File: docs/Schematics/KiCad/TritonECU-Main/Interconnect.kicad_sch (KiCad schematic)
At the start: 3 parts, among them J1 EEC-V 104

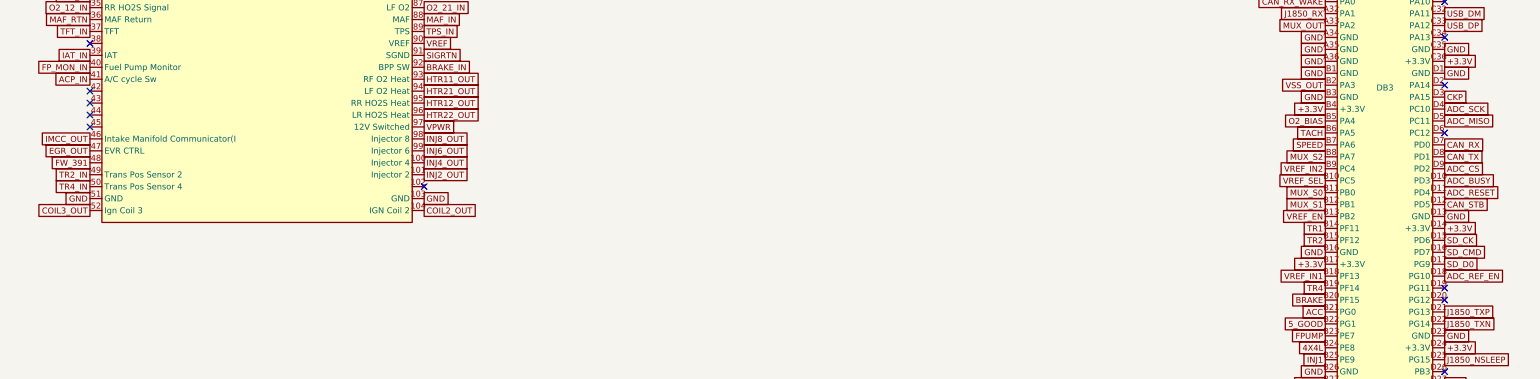
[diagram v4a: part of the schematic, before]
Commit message: Carrier: Comms sheet (SCP, CAN, USB-C, microSD)
SCP: DRV8837 (coast = passive, nSLEEP 10k low), 100R per line, NUP2105L;
TLV7031 RX with the corrected 100k:100k divider to GND, MM3Z3V3 clamps,
4.7M hysteresis, 100R + SMF3.3A out. CAN: TJA1042T/3, RXD also to PA0
WKUP1, split termination 2 x 60.4R + 4.7n, NUP2105L; bus on EEC-V 42/43
(added terminals, unused cavities). USB-C device (USB4105, 5.1k CC,
USBLC6-2SC6, VBUS sense). microSD Molex 104031 on SDMMC2 1-bit, powered
through a TPS22917 on SD_PWR_EN (PG11): 3.3 V is always on.

USB-C on the right board edge; microSD parked off-board (wider than the
free strip). Scoped DRC rule for the USB4105 land pattern.

Co-Authored-By: Claude Opus 5.5 <noreply@anthropic.com>
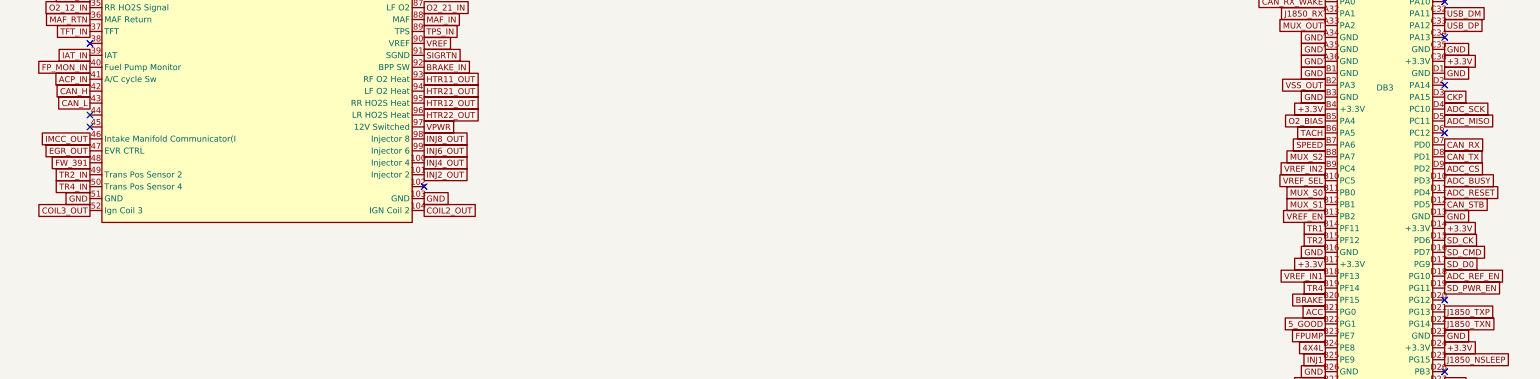
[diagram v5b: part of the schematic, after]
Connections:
- net CAN_H: now reaches J1.42
- net CAN_L: now reaches J1.43
- net SD_PWR_EN: now reaches DB3.D19 (PG11)
- no-connect marks 38 -> 35

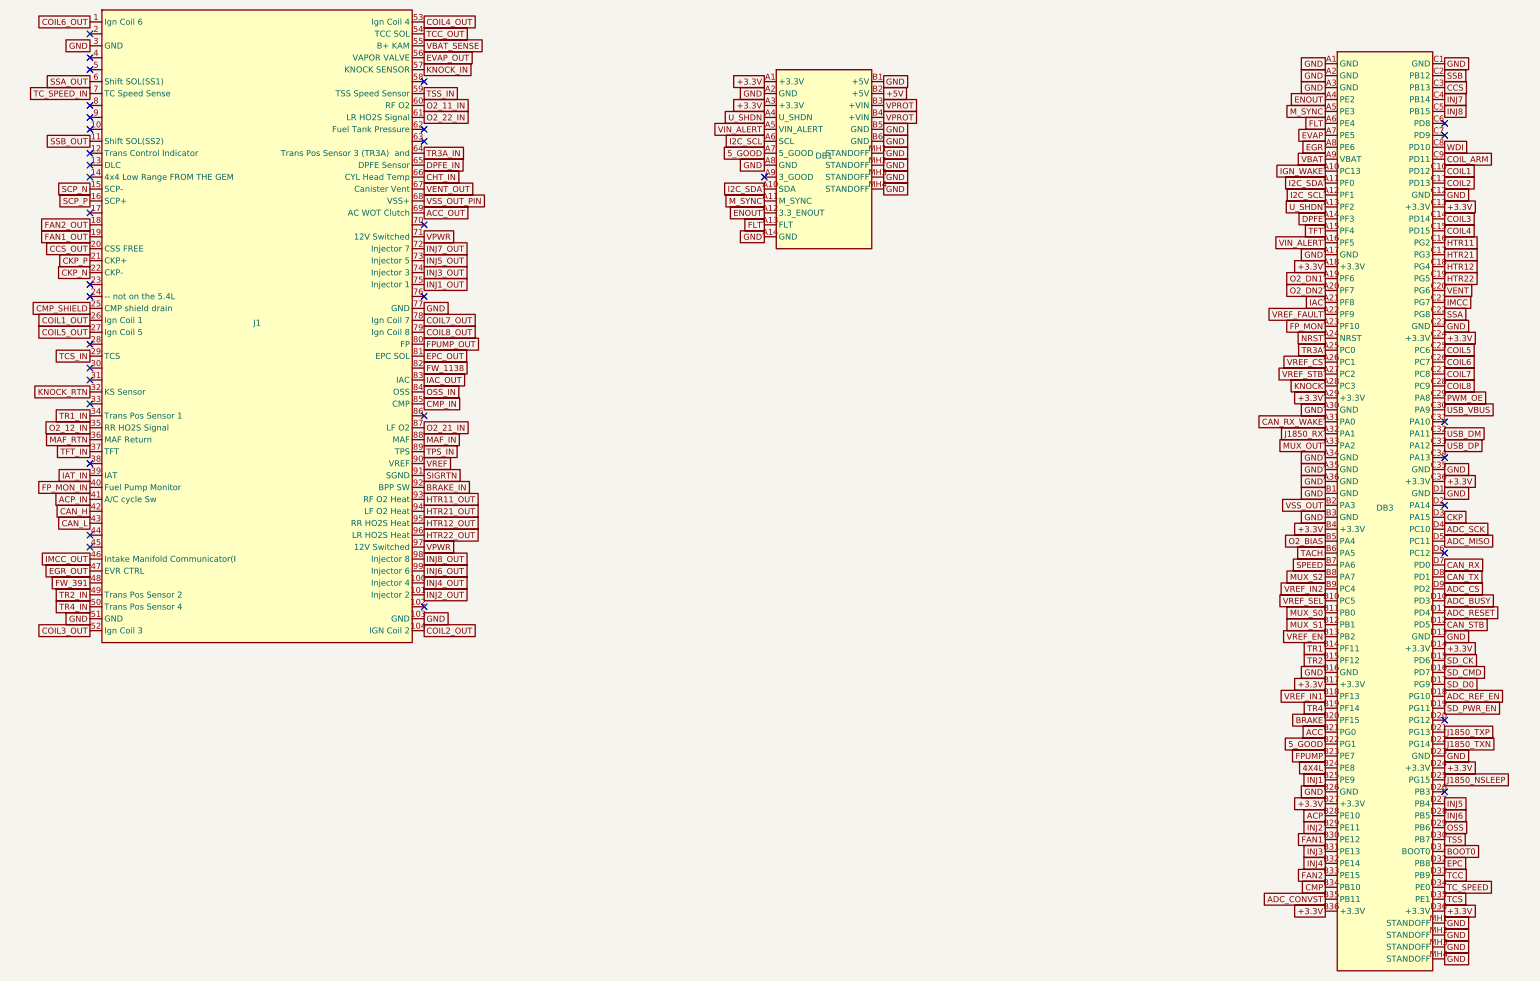
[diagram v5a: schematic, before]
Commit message: Carrier: Inputs sheet and switched rails for sleep
Inputs: one network per switch input - 4.7k pull-up to VPWR (ground-
switched only; VPWR so a TR bit closed in Park draws nothing parked),
SMF24A, 33k/15k, 10n, BAT54J to 3.3 V. TR1/2/4 and 4X4L ground-switched,
TR3A/BRAKE/ACP/TCS 12 V high-side. 4X4L mapped to EEC-V pin 14
(findings sec.14). IGN_WAKE from VPWR into PC13/WKUP4. TACH/SPEED bench
header, BOOT0 DFU solder jumper.

Switched rails: +5V and +3.3V stay up parked, so two TPS22917 load
switches on SW_RAIL_EN (PG12, 100k down) make +5V_SW / +3.3V_SW for the
running-only loads: 74HCT541 x3 and OE pull-ups, MAX9926 x3 and COUT
pull-ups, ADS8588H, OPA2376 x2, O2 bias, knock block, 74HC4051, TPS2H160B
FAULT pull-up, TFT pull-up. MCU, watchdog, CAN, SCP RX, clamps stay on.

gen_carrier_pcb.py: packer steps around existing parts, fills several
rects in turn, parks overflow below earlier parked parts.

Co-Authored-By: Claude Opus 5.5 <noreply@anthropic.com>
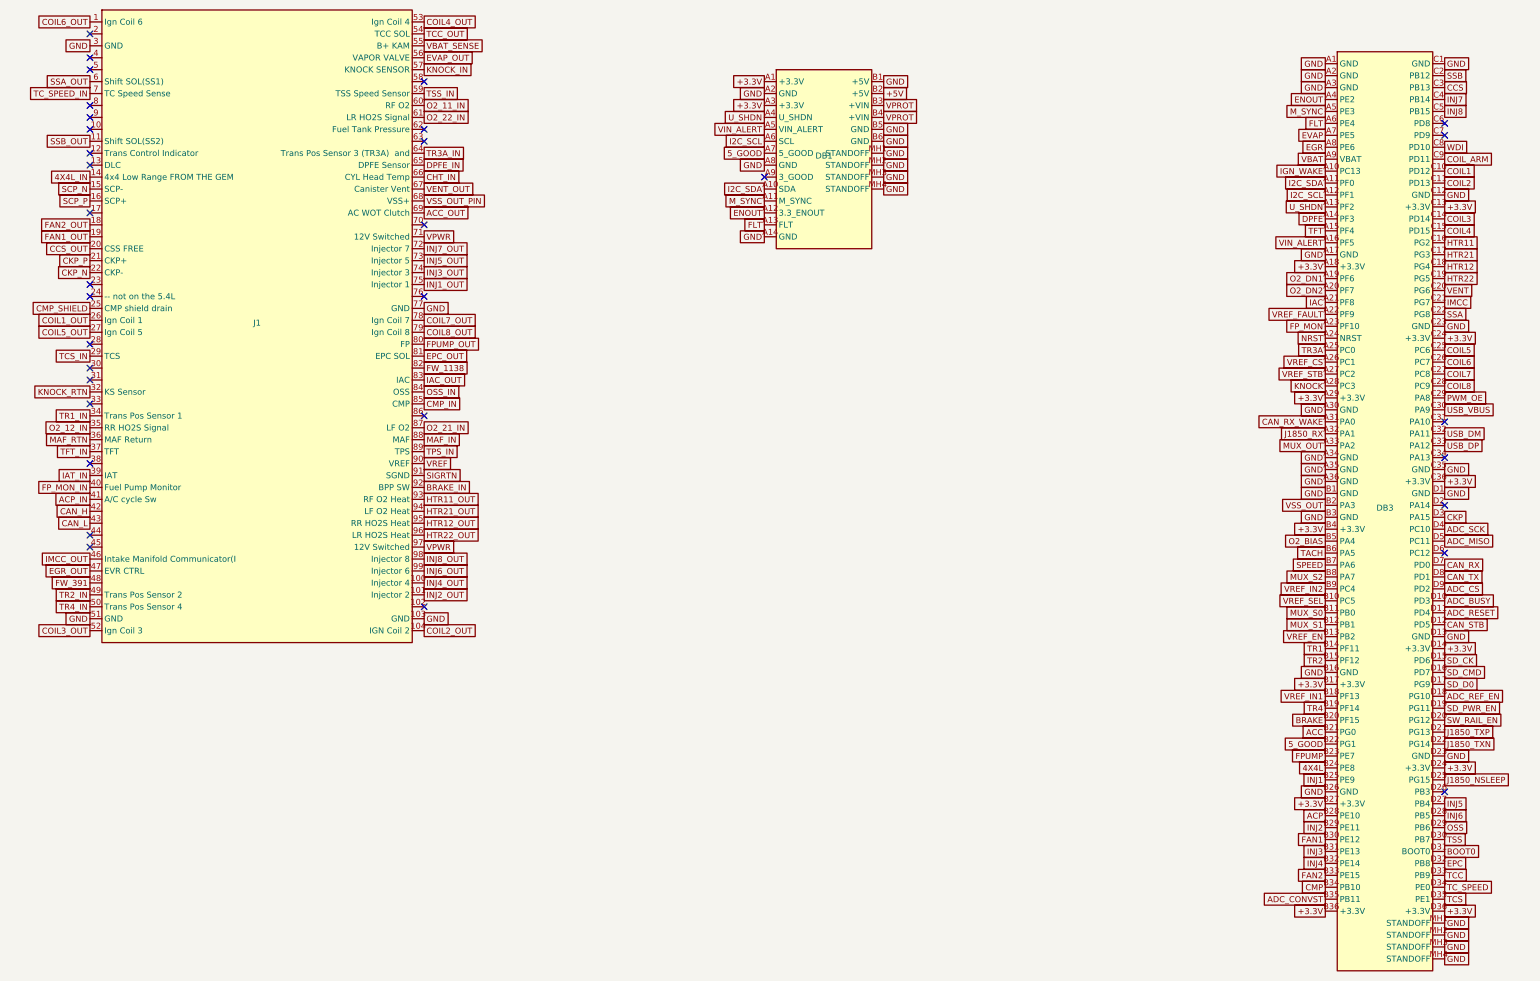
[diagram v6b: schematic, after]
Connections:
- net 4X4L_IN: now reaches J1.14 (4x4 Low Range FROM THE GEM)
- net SW_RAIL_EN: now reaches DB3.D20 (PG12)
- no-connect marks 35 -> 33
